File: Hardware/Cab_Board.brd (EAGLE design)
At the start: 152.9 x 71.1 mm, 95 parts, among them J1 3PCV-04-006, J6 3PCV-03-006, SW1 MF-SW-TACT-4.2MM, SW2 MF-SW-TACT-4.2MM, SW3 MF-SW-TACT-4.2MM, U1 P8X32A-Q44, U2 LT8672EMS#PBF, U27 FXOS8700CQR1, U29 MAX11613EUA+, U3 IPD100N06S403ATMA2, U4 LT8614IUDC#PBF, U7 CAT24C512WI-GT3, X1 6.0MHz

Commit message: cleaing up schematic more.
8 analog inputs
0-5V Analog in
Thermistors
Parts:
- removed 12V, GND: (no value), PP_Connectors:KEYSTONE_5115-5119
- removed C11, C12, C20, C25, C26, C37, C40, C41, C43, C7: 0.1uF, PP_Passives:0805
- removed C18: 1000uF, PP_Passives:12.5MM_CAP_PTH
- removed C19: 220uF, PP_Passives:10MM_CAP_SMD
- removed C36: 4.7uF, PP_Passives:1206
- removed C6: 10uF, PP_Passives:1206
- removed DISP1: 61201621621, PP_Displays:CU40045-UW1J
- removed J1: 3PCV-04-006, PP_Connectors:3PCV-04-006
- removed J6: 3PCV-03-006, PP_Connectors:3PCV-03-006
- removed R10, R12, R13, R17, R9: 10K, PP_Passives:0603
- removed R14, R18, R25, R26, R27, R3, R4, R5, R6, R7, R8: 100, PP_Passives:0603
- removed R15, R16, R19, R20: 15K, PP_Passives:0603
- removed R21, R22, R23, R24: 4.7K, PP_Passives:0603
- removed SW1, SW2, SW3: MF-SW-TACT-4.2MM, MF_Switches:TACT4.2MM
- removed SW_D, SW_S, SW_U: 1546215-2, PP_Connectors:1546215-2
- removed TVS1: V18AUMLA2220H, PP_Passives:2220
- removed U27: FXOS8700CQR1, PP_Sensors:FXOS8700CQR1
- removed U29: MAX11613EUA+, PP_AnalogIC:MAX11613_UMAX-8
- added C24, C27, C30: 1uF, PP_Passives:0805
- added C28: 4.7pF, PP_Passives:0603
- added C29: 0.1uF, PP_Passives:0603
- added C32: 10nF, PP_Passives:0603
- added C33: 47uF, PP_Passives:1210
- added J2: TBL009-254-02GY-2GY, PP_Connectors:TBL009-254-02GY-2GY
- added L3: IHLP2525CZER4R7M01, PP_Passives:IHLP-2525
- added R29: 41.2K, PP_Passives:0603
- added R30: 1M, PP_Passives:0603
- added R31: 243K, PP_Passives:0603
- added U5: LT8614IUDC#PBF, PP_PowerIC:LT8614_QFN-18
- D2: value VS-12CWQ10FN-M3 -> BAT54S; device PP_Passives:D-PAK(TO-252AA) -> PP_Passives:SOT-23
- moved D2 273.2 mm to (-47.2, -204.7), turned to 0 degrees
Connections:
- net 165_CLK renamed P13
- net 165_DATA renamed P11
- net 165_LOAD renamed P12
- net 595_CLK renamed P16
- net 595_DATA renamed P14
- net 595_LAT renamed P15
- net TC_CS_0 renamed P22
- net TC_CS_1 renamed P23
- net TC_CS_2 renamed P24
- net TC_CS_3 renamed P25
- net TC_SCK renamed P27
- net TC_SO renamed P26
- removed net 12V: 12V.P$1, C18.POS, C19.POS, D2.PAD-4
- removed net 12V_BATT: D2.1, D2.3, J6.1, TVS1.P$2
- removed net 5V: C6.1, DISP1.P$13
- removed net A0: C7.1, R15.1, R24.2, U29.P$1
- removed net A1: C11.1, R16.1, R23.2, U29.P$2
- removed net A2: C12.1, R19.1, R22.2, U29.P$3
- removed net A3: C20.1, R20.1, R21.2, U29.P$4
- removed net D4: DISP1.P$3, R6.2
- removed net D5: DISP1.P$4, R5.2
- removed net D6: DISP1.P$1, R4.2
- removed net D7: DISP1.P$2, R3.2
- removed net DOME_PWR: J6.3
- removed net E1: DISP1.P$10, R8.2
- removed net E2: DISP1.P$16, R7.2
- removed net N$1: J1.1, R15.2
- removed net N$10: R25.2, SW_U.P$1
- removed net N$11: R26.2, SW_S.P$1
- removed net N$12: R27.2, SW_D.P$1
- removed net N$3: J1.2, R16.2
- removed net N$4: J1.3, R19.2
- removed net N$6: J1.4, R20.2
- removed net N$7: C26.1, U27.P$2
- removed net N$8: C40.1, U27.P$8
- removed net PROP_D4: R6.1, U1.44
- removed net PROP_D5: R5.1, U1.1
- removed net PROP_D6: R4.1, U1.42
- removed net PROP_D7: R3.1, U1.43
- removed net PROP_E1: R8.1, U1.2
- removed net PROP_E2: R7.1, U1.9
- removed net PROP_R/W: R14.1, U1.3
- removed net PROP_RS: R18.1, U1.4
- removed net R/W: DISP1.P$9, R14.2
- removed net RS: DISP1.P$12, R18.2
- removed net SW_D: R27.1, R9.2, SW3.P$1, U1.22
- removed net SW_S: R10.2, R26.1, SW2.P$1, U1.23
- removed net SW_U: R17.2, R25.1, SW1.P$1, U1.24
- new net 5.0V: C28.1, C33.1, L3.P$2, R30.2, U5.1
- new net BST1: C29.1, U5.3
- new net FB1: C28.2, R30.1, R31.2, U5.20
- new net INTVCC1: C30.2, U5.2
- new net P1: U1.42
- new net P19: U1.22
- new net P2: U1.43
- new net P20: U1.23
- new net P21: U1.24
- new net P3: U1.44
- new net P4: U1.1
- new net P5: U1.2
- new net P6: U1.3
- new net P7: U1.4
- new net P8: U1.9
- new net RT1: R29.2, U5.15
- new net SW1: C29.2, L3.P$1, U5.21, U5.22, U5.8, U5.9
- new net TR/SS1: C32.2, U5.16
- net 3.3V: no longer C25.1, C36.1, C37.1, C41.1, C43.1, R10.1, R12.2, R13.2, R17.1, R9.1, U27.P$1, U27.P$14, U29.P$8
- net GND: now also C24.2, C27.2, C30.1, C32.1, C33.2, J2.2A, J2.2B, R29.1, R31.1, U5.10, U5.11, U5.18, U5.6, U5.7; no longer C11.2, C12.2, C18.NEG, C19.NEG, C20.2, C25.2, C26.2, C36.2, C37.2, C40.2, C41.2, C43.2, C6.2, C7.2, DISP1.P$14, DISP1.P$5, DISP1.P$6, DISP1.P$7, DISP1.P$8, GND.P$1, J6.2, R21.1, R22.1, R23.1, R24.1, SW1.P$4, SW2.P$4, SW3.P$4, SW_D.P$2, SW_S.P$2, SW_U.P$2, TVS1.P$1, U27.P$10, U27.P$12, U27.P$13, U27.P$16, U27.P$3, U27.P$5, U27.P$7, U29.P$7
- net N$13: now also C24.1, C27.1, U5.13, U5.14, U5.4
- net SCL: no longer R12.1, U27.P$4, U29.P$5
- net SDA: no longer R13.1, U27.P$6, U29.P$6
- net VIN: now also J2.1A, J2.1B
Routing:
- net PROP_E2: track 97.4 -> 0.00 mm
- net P8: track 0.00 -> 96.7 mm
- net PROP_RS: track 86.8 -> 0.00 mm
- net P7: track 0.00 -> 86.1 mm
- net PROP_R/W: track 83.8 -> 0.00 mm
- net P6: track 0.00 -> 83.1 mm
- net PROP_E1: track 81.0 -> 0.00 mm
- net P5: track 0.00 -> 80.0 mm
- net PROP_D5: track 77.8 -> 0.00 mm
- net 3.3V: track 205.5 -> 128.6 mm, vias 18 -> 8
- net PROP_D4: track 74.3 -> 0.00 mm
- net P4: track 0.00 -> 73.8 mm
- net PROP_D7: track 73.0 -> 0.00 mm
- net PROP_D6: track 71.7 -> 0.00 mm
- net P3: track 0.00 -> 69.3 mm
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
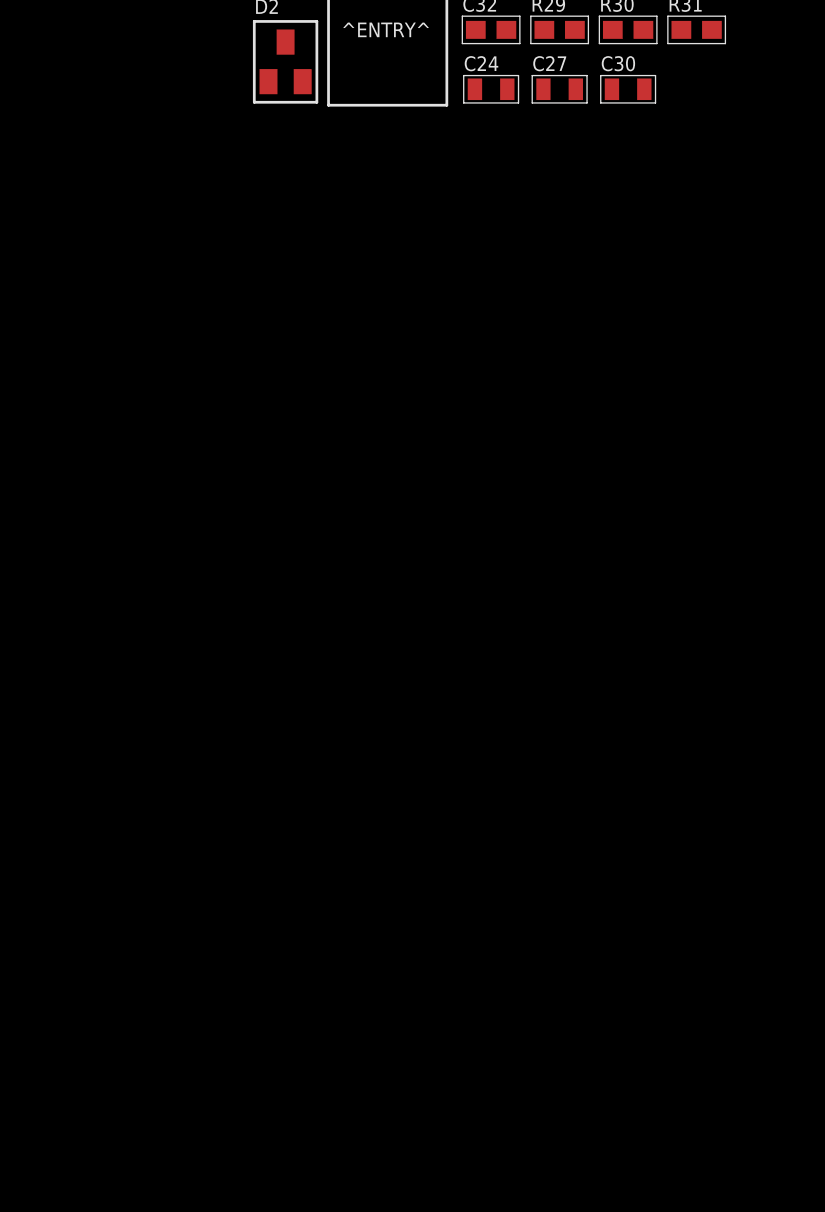
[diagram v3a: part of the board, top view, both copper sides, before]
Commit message: added LTC2986HLX#PBF
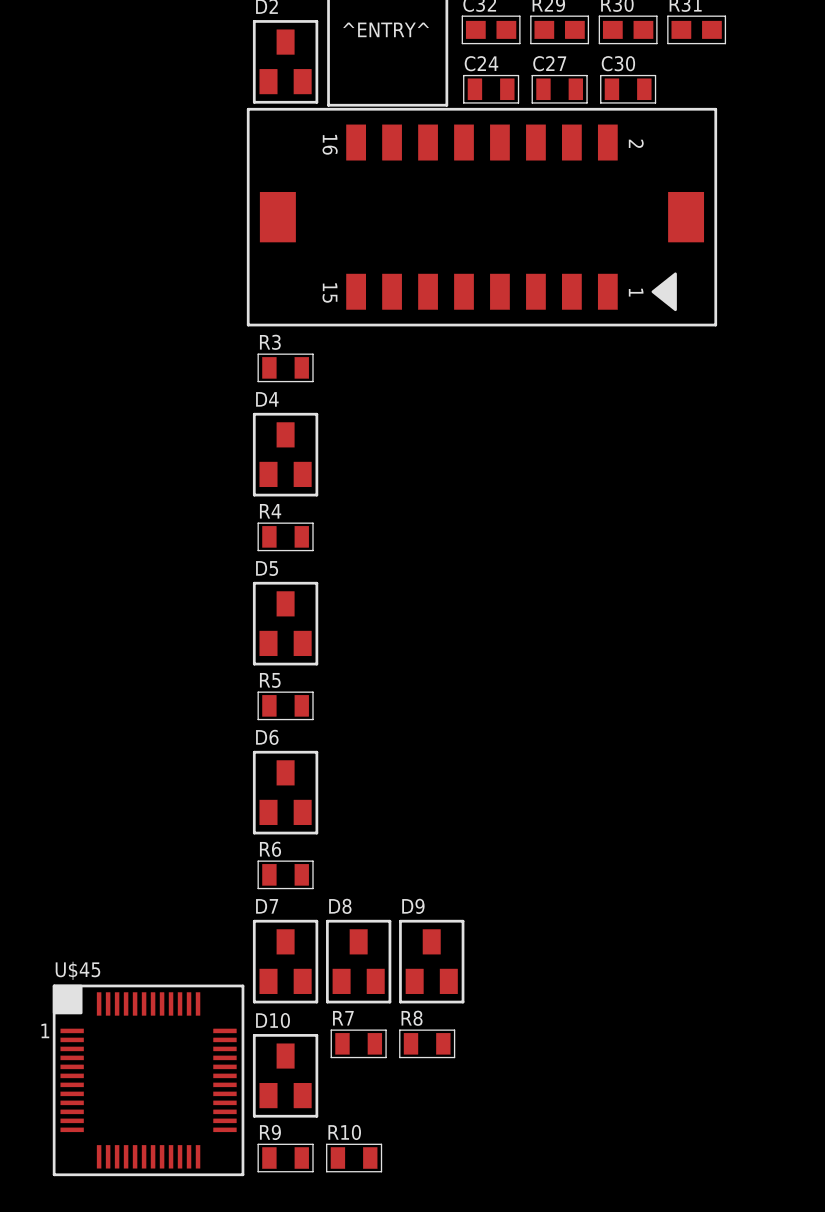
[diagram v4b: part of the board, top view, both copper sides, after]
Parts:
- added D10, D4, D5, D6, D7, D8, D9: BAT54S, PP_Passives:SOT-23
- added J1: DF11G-16DP-2V(50), PP_Connectors:DF11G-16DP-2V(50)
- added R10, R3, R4, R5, R6, R7, R8, R9: 330, PP_Passives:0805
- added U$45: LTC2986HLX#PBF, PP_Sensors:LQFP-48
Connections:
- removed net P0: U1.41
- removed net P1: U1.42
- new net ANALOG_MCU_0: D2.3, R3.1
- new net ANALOG_MCU_1: D4.3, R4.1
- new net ANALOG_MCU_2: D5.3, R5.1
- new net ANALOG_MCU_3: D6.3, R6.1
- new net ANALOG_MCU_4: D7.3, R7.1
- new net ANALOG_MCU_5: D8.3, R8.1
- new net ANALOG_MCU_6: D9.3, R9.1
- new net ANALOG_MCU_7: D10.3, R10.1
- new net ANALOG_WORLD_0: R3.2
- new net ANALOG_WORLD_1: R4.2
- new net ANALOG_WORLD_2: R5.2
- new net ANALOG_WORLD_3: R6.2
- new net ANALOG_WORLD_4: R7.2
- new net ANALOG_WORLD_5: R8.2
- new net ANALOG_WORLD_6: R9.2
- new net ANALOG_WORLD_7: R10.2
- new net GPIO0: J1.P$11
- new net GPIO1: J1.P$12
- new net GPIO2: J1.P$9
- new net GPIO3: J1.P$10
- new net GPIO4: J1.P$13
- new net LCD_RX: J1.P$1, U1.42
- new net LCD_TX: J1.P$2, U1.41
- net 5.0V: now also D10.1, D2.1, D4.1, D5.1, D6.1, D7.1, D8.1, D9.1, J1.P$16
- net GND: now also D10.2, D2.2, D4.2, D5.2, D6.2, D7.2, D8.2, D9.2, J1.P$15
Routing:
- net P1: track 64.7 -> 0.00 mm
- net LCD_RX: track 0.00 -> 64.7 mm

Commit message: Control side of LTC2986HLX done.
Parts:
- removed D10, D2, D4, D5, D6, D7, D8, D9: BAT54S, PP_Passives:SOT-23
- removed R10, R6, R7, R8, R9: 330, PP_Passives:0805
- removed U$45: LTC2986HLX#PBF, PP_Sensors:LQFP-48
- added C11, C12, C18, C19, C35, C36, C6, C7: 0.1uF, PP_Passives:0805
- added C20: 1uF, PP_Passives:0805
- added C25, C26, C34: 10uF, PP_Passives:1210
- added U6: IPD100N06S403ATMA2, PP_DiscreteSemi:TO-252-3
- added U8: TXB0104DR, PP_DigitalIC:TXB0104_SOIC-14
- R3, R4: value 330 -> 10K; device PP_Passives:0805 -> PP_Passives:0603
- R5: value 330 -> 18K; device PP_Passives:0805 -> PP_Passives:0603
- U2: value LT8672EMS#PBF -> CAT24C512WI-GT3; device PP_PowerIC:LT8672_MSOP-10 -> PP_DigitalIC:SOIC-8_W
- U3: value IPD100N06S403ATMA2 -> LT8672EMS#PBF; device PP_DiscreteSemi:TO-252-3 -> PP_PowerIC:LT8672_MSOP-10
- U7: value CAT24C512WI-GT3 -> LTC2986HLX-1#PBF; device PP_DigitalIC:SOIC-8_W -> PP_Sensors:LQFP-48
- moved U7 320.5 mm to (-54.9, -261.4)
- moved U2 169.2 mm to (52.6, 40.6)
- moved R4 86.9 mm to (-67.3, -315.7)
- moved R3 86.4 mm to (-67.3, -305.8)
- moved R5 81.0 mm to (-67.3, -319.0)
- moved U3 9.45 mm to (-9.40, -116.8)
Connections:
- removed net ANALOG_MCU_0: D2.3, R3.1
- removed net ANALOG_MCU_1: D4.3, R4.1
- removed net ANALOG_MCU_2: D5.3, R5.1
- removed net ANALOG_MCU_3: D6.3, R6.1
- removed net ANALOG_MCU_4: D7.3, R7.1
- removed net ANALOG_MCU_5: D8.3, R8.1
- removed net ANALOG_MCU_6: D9.3, R9.1
- removed net ANALOG_MCU_7: D10.3, R10.1
- removed net ANALOG_WORLD_0: R3.2
- removed net ANALOG_WORLD_1: R4.2
- removed net ANALOG_WORLD_2: R5.2
- removed net ANALOG_WORLD_3: R6.2
- removed net ANALOG_WORLD_4: R7.2
- removed net ANALOG_WORLD_5: R8.2
- removed net ANALOG_WORLD_6: R9.2
- removed net ANALOG_WORLD_7: R10.2
- removed net P10: U1.11
- removed net P11: U1.12
- removed net P12: U1.13
- removed net P7: U1.4
- removed net P8: U1.9
- removed net P9: U1.10
- new net 3.3V_!CS: U1.4, U8.2
- new net 3.3V_SCK: U1.11, U8.5
- new net 3.3V_SDI: U1.9, U8.3
- new net 3.3V_SDO: U1.10, U8.4
- new net 5V_!CS: U7.P$41, U8.13
- new net 5V_SCK: U7.P$38, U8.10
- new net 5V_SDI: U7.P$40, U8.12
- new net 5V_SDO: U7.P$39, U8.11
- new net LTC2986_INTERRUPT: R4.1, R5.2, U1.13
- new net N$1: C19.1, U7.P$11
- new net N$12: R4.2, U7.P$37
- new net N$3: C20.1, U7.P$13, U7.P$14
- new net N$4: C26.1, U7.P$46
- new net N$6: C25.2, U7.P$47
- new net N$7: C25.1, U7.P$48
- new net N$8: C34.1, U7.P$43
- new net SPI_LEVEL_SHIFTER_OE: R3.2, U1.12, U8.8
- net 3.3V: now also C36.1, U2.8, U8.1; no longer U7.8
- net 5.0V: now also C11.1, C12.1, C18.1, C35.1, C6.1, C7.1, U7.P$2, U7.P$4, U7.P$42, U7.P$45, U7.P$6, U7.P$8, U8.14; no longer D10.1, D2.1, D4.1, D5.1, D6.1, D7.1, D8.1, D9.1
- net GND: now also C11.2, C12.2, C18.2, C19.2, C20.2, C26.2, C34.2, C35.2, C36.2, C6.2, C7.2, R3.1, R5.1, U2.3, U2.7, U3.2, U3.4, U7.P$1, U7.P$12, U7.P$15, U7.P$26, U7.P$27, U7.P$28, U7.P$29, U7.P$3, U7.P$30, U7.P$31, U7.P$32, U7.P$33, U7.P$34, U7.P$35, U7.P$44, U7.P$5, U7.P$7, U7.P$9, U8.7; no longer D10.2, D2.2, D4.2, D5.2, D6.2, D7.2, D8.2, D9.2, U7.2, U7.3, U7.4, U7.7
- net N$13: now also U3.8, U6.PAD; no longer U2.8, U3.PAD
- net N$14: now also U3.7; no longer U2.7
- net N$15: now also U3.6; no longer U2.6
- net N$2: now also U3.10, U6.1; no longer U2.10, U3.1
- net SCL: now also U2.6; no longer U7.6
- net SDA: now also U2.5; no longer U7.5
- net VIN: now also U3.9, U6.3; no longer U2.9, U3.3
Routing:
- net P8: track 96.7 -> 0.00 mm
- net 3.3V_SDI: track 0.00 -> 96.7 mm
- net P7: track 86.1 -> 0.00 mm
- net 3.3V_!CS: track 0.00 -> 86.1 mm
- net P10: track 60.7 -> 0.00 mm, vias 2 -> 0
- net 3.3V_SCK: track 0.00 -> 60.7 mm, vias 0 -> 2
- net P9: track 58.1 -> 0.00 mm
- net 3.3V_SDO: track 0.00 -> 58.1 mm
- net P12: track 46.2 -> 0.00 mm
- net LTC2986_INTERRUPT: track 0.00 -> 46.2 mm
- net SPI_LEVEL_SHIFTER_OE: track 0.00 -> 35.0 mm
- net P11: track 35.0 -> 0.00 mm
